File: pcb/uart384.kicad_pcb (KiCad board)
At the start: 2 copper layers, 54.1 x 23.5 mm, 36 parts, among them IC1 ICE40LP384-SG32, J1 USB_A, J2 TC2050, J3 Conn_02x07_Odd_Even, J4 TC2050_ext, SW1 SW_Push, U1 AT25DF256-SSHN, U2 CP2102-QFN28, U3 MIC5365-1.2YC5, Y1 XO32

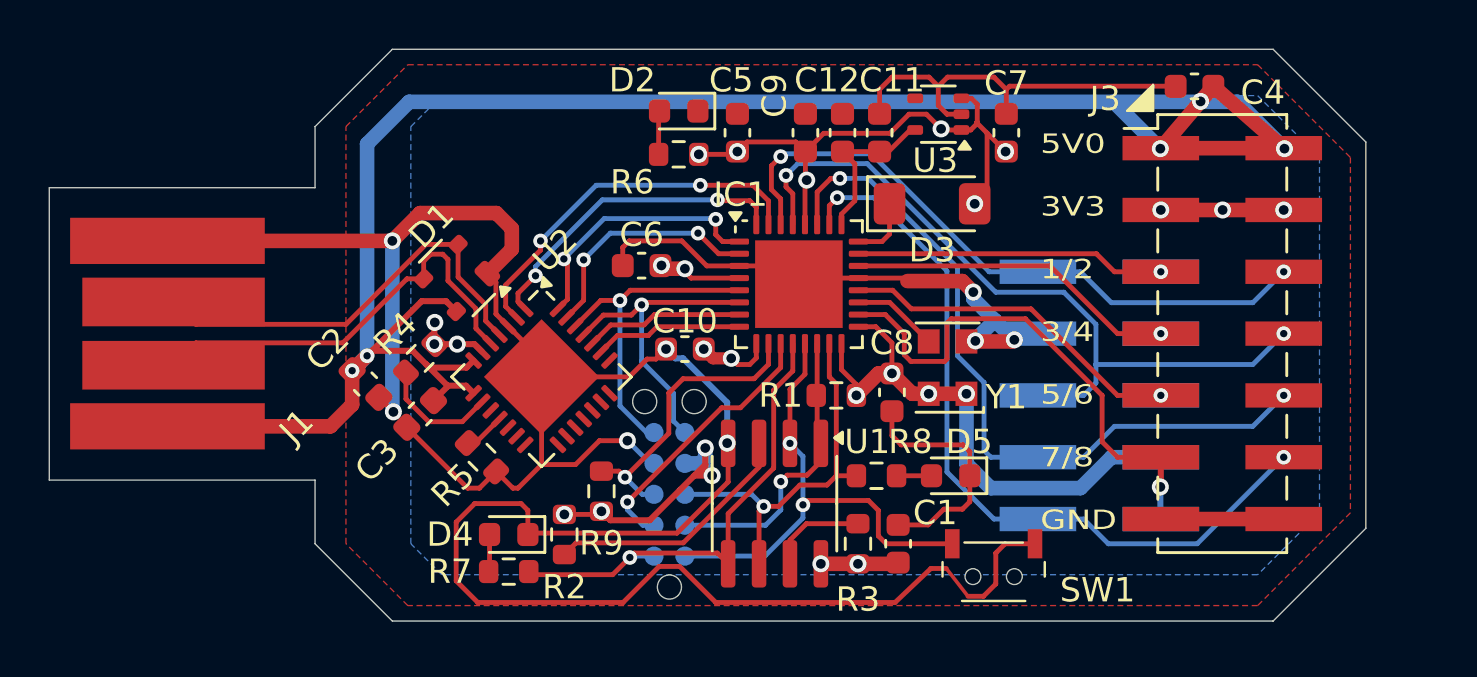
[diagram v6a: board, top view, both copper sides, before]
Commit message: PCB: major hardware revision 2.0~DEV: restructure FPGA pinout, fully reroute.
- re-map iCE40LP384 pins for GPIO 1-8, UART, CLK to optimize usability
  and allow experiments with LVDS pairs.

- allow voltage selection for LVDS pins (bank 3) between 3v3 (default)
  and 2v5 (untested, only via diode drop!).

- make programming pad TC2050 fully available, take care not to place
  components on other side of it.

- fully place&route, then optimization of PCB, planes etc.

- provide PCF files for both hardware revisions
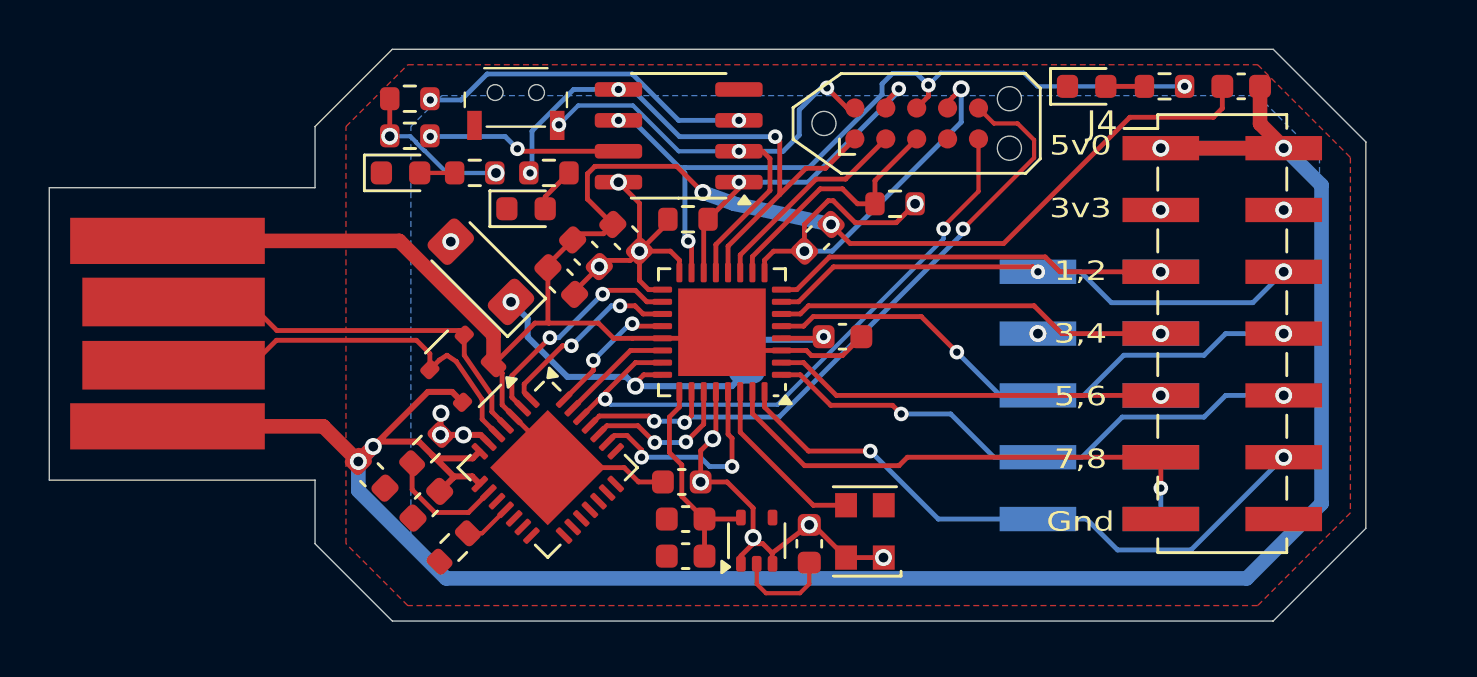
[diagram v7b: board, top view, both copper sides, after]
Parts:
- added JP1: SolderJumper_3_Bridged12, Jumper:SolderJumper-3_P1.3mm_Bridged2Bar12_RoundedPad1.0x1.5mm, B.Cu at (104.9, 76.5)
- J2: moved to F.Cu
- moved SW1 27.9 mm to (95.4, 66.3), turned to 0 degrees
- moved R3 24.9 mm to (91.1, 68.1), turned to 0 degrees
- moved R8 19.9 mm to (122.1, 66.0), turned to 180 degrees
- moved C10 19.1 mm to (102.4, 85.3), turned to 180 degrees
- moved U3 19.0 mm to (105.3, 84.7), turned to 90 degrees
- moved R2 19.0 mm to (91.1, 66.5), turned to 0 degrees
- moved D3 18.8 mm to (94.0, 73.7), turned to 135 degrees
- moved C6 18.7 mm to (107.5, 84.8), turned to -90 degrees
- moved J2 18.3 mm to (111.9, 67.6), turned to 0 degrees
- moved C1 17.5 mm to (98.3, 72.9), turned to 135 degrees
- moved C12 17.1 mm to (102.4, 83.8), turned to 0 degrees
- moved D5 16.9 mm to (118.9, 66.0), turned to 0 degrees
- moved R9 16.9 mm to (111.0, 70.9), turned to 180 degrees
- moved R7 16.5 mm to (96.8, 69.6), turned to 0 degrees
- moved U1 15.6 mm to (102.1, 68.1), turned to 180 degrees
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- renumbered C11 to C10, C10 to C11, C7 to C6, C6 to C7
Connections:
- C11 pad 1: +3V3 -> GND
- C11 pad 2: GND -> Net-(IC1-VCC_IO3)
- IC1 pad 1: /UART_DTR -> /GPIO6
- IC1 pad 18: /GPIO7 -> /UART_RI
- IC1 pad 19: /CLK -> /UART_DCD
- IC1 pad 2: /UART_DSR -> /GPIO5
- IC1 pad 20: /GPIO5 -> /UART_DTR
- IC1 pad 22: /GPIO3 -> /UART_DSR
- IC1 pad 23: /GPIO1 -> /UART_TXD
- IC1 pad 26: /GPIO8 -> /UART_RXD
- IC1 pad 27: /GPIO6 -> /UART_RTS
- IC1 pad 29: /GPIO4 -> /UART_CTS
- IC1 pad 30: /GPIO2 -> /CLK
- IC1 pad 31: /UART_RI -> /GPIO7
- IC1 pad 32: /UART_DCD -> /GPIO8
- IC1 pad 4: +3V3 -> Net-(IC1-VCC_IO3)
- IC1 pad 5: /UART_TXD -> /GPIO4
- IC1 pad 6: /UART_RXD -> /GPIO3
- IC1 pad 7: /UART_RTS -> /GPIO2
- IC1 pad 8: /UART_CTS -> /GPIO1
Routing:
- net GND: track 158.3 -> 85.9 mm, vias 8 -> 3
- net /SCK: track 15.8 -> 32.2 mm, vias 1 -> 4
- net /UART_RXD: track 12.9 -> 28.1 mm, vias 1 -> 3
- net +3V3: track 73.8 -> 58.9 mm, vias 26 -> 19
- net /UART_TXD: track 13.5 -> 25.9 mm, vias 1 -> 2
- net +2V5: track 2.65 -> 13.9 mm, vias 0 -> 2
- net /GPIO4: track 32.2 -> 23.2 mm
- net VBUS: track 87.0 -> 95.0 mm, vias 5 -> 4
- net /GPIO6: track 30.3 -> 23.1 mm
- net /UART_RI: track 15.5 -> 9.35 mm
- net /GPIO8: track 31.8 -> 26.0 mm
- net /UART_DTR: track 10.9 -> 5.61 mm
- net /UART_DCD: track 13.2 -> 7.91 mm
- net /UART_DSR: track 9.86 -> 4.67 mm, vias 2 -> 0
- net Net-(IC1-VCC_IO3): track 0.00 -> 4.97 mm, vias 0 -> 1
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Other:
- board text added: "2v5"
- board text added: "5v0 3v3 1,2 3,4 5,6 7,8 Gnd"
- board text added: "BANK3"
- board text added: "UART384"
- board text added: "v2.0~ by dpiegdon"
- board text removed: "5V0 3V3 1/2 3/4 5/6 7/8 GND"
- board text removed: "UART384 v1.1 by dpiegdon"

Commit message: PCB: add voltage regulator choices for VCC_IO3, selectable via jumper, DNP
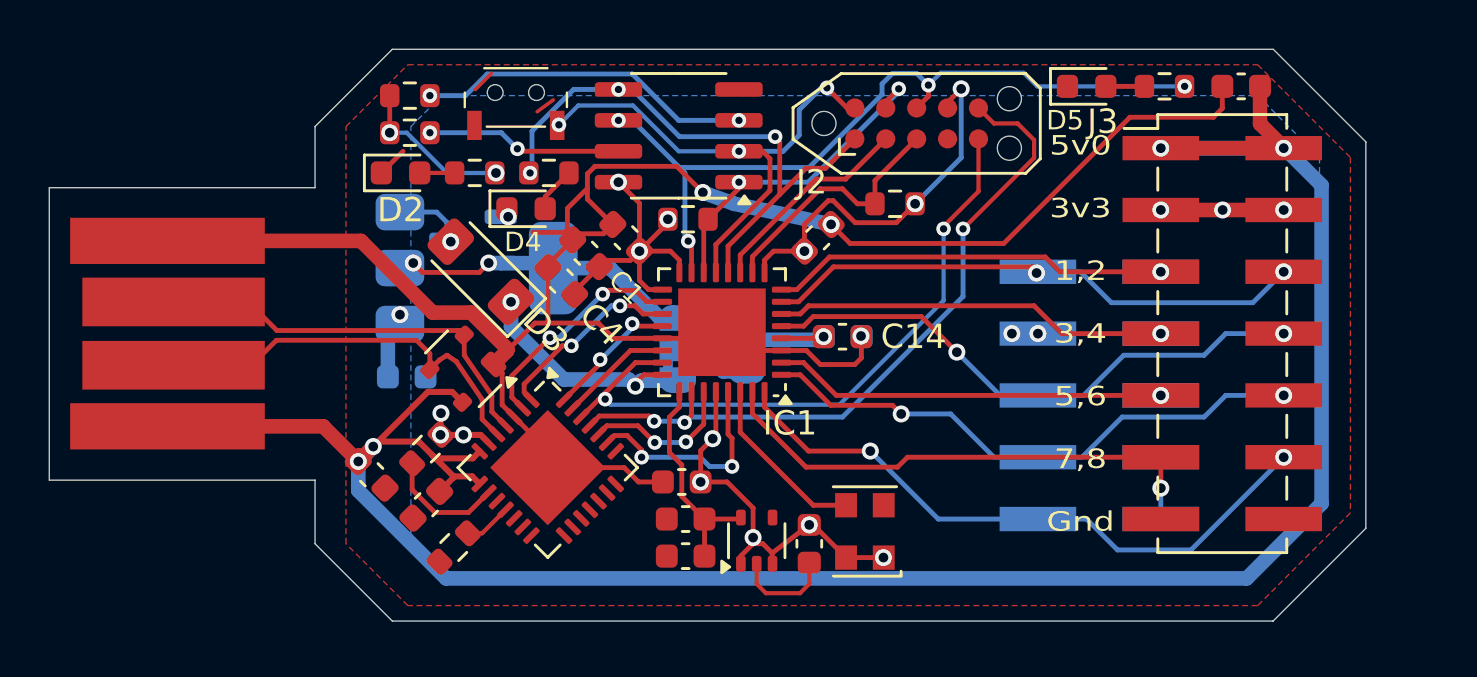
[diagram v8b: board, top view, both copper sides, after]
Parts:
- added C11: 1u, Capacitor_SMD:C_0603_1608Metric, B.Cu at (90.9, 78.0)
- added C12: 1u, Capacitor_SMD:C_0603_1608Metric, B.Cu at (108.9, 76.3)
- added JP1: VSEL2, Jumper:SolderJumper-3_P1.3mm_Bridged2Bar12_RoundedPad1.0x1.5mm, B.Cu at (102.1, 76.8)
- added U4: AMS1117-2.5, Package_TO_SOT_SMD:SOT-223-3_TabPin2, B.Cu at (93.8, 73.5)
- added U5: XC6206P182MR, Package_TO_SOT_SMD:SOT-23-3, B.Cu at (93.7, 72.3)
- JP2: renamed from JP1; value SolderJumper_3_Bridged12 -> VSEL1
- moved R3 0.13 mm to (91.1, 67.9)
- moved R2 0.13 mm to (91.1, 66.4)
- renumbered C9 to C10, C12 to C13, C11 to C14, C5 to C4, C6 to C5, C10 to C6, C4 to C8, C8 to C9, J4 to J3, J3 to J4
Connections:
- net Net-(IC1-VCC_IO3) renamed Vdrive
- JP2 pad 3: +2V5 -> Net-(JP1-C)
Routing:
- net Net-(JP1-B): track 0.00 -> 12.7 mm, vias 0 -> 2
- net GND: track 85.9 -> 98.3 mm, vias 3 -> 7
- net +3V3: track 58.9 -> 62.5 mm, vias 19 -> 20
- net Net-(JP1-C): track 0.00 -> 3.22 mm
- net +2V5: track 13.9 -> 11.1 mm
- net /UART_RXD: track 28.1 -> 29.6 mm
- net /UART_TXD: track 25.9 -> 27.4 mm
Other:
- board text removed: "2v5"
- board text removed: "BANK3"
